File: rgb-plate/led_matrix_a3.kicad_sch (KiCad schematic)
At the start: 32 parts

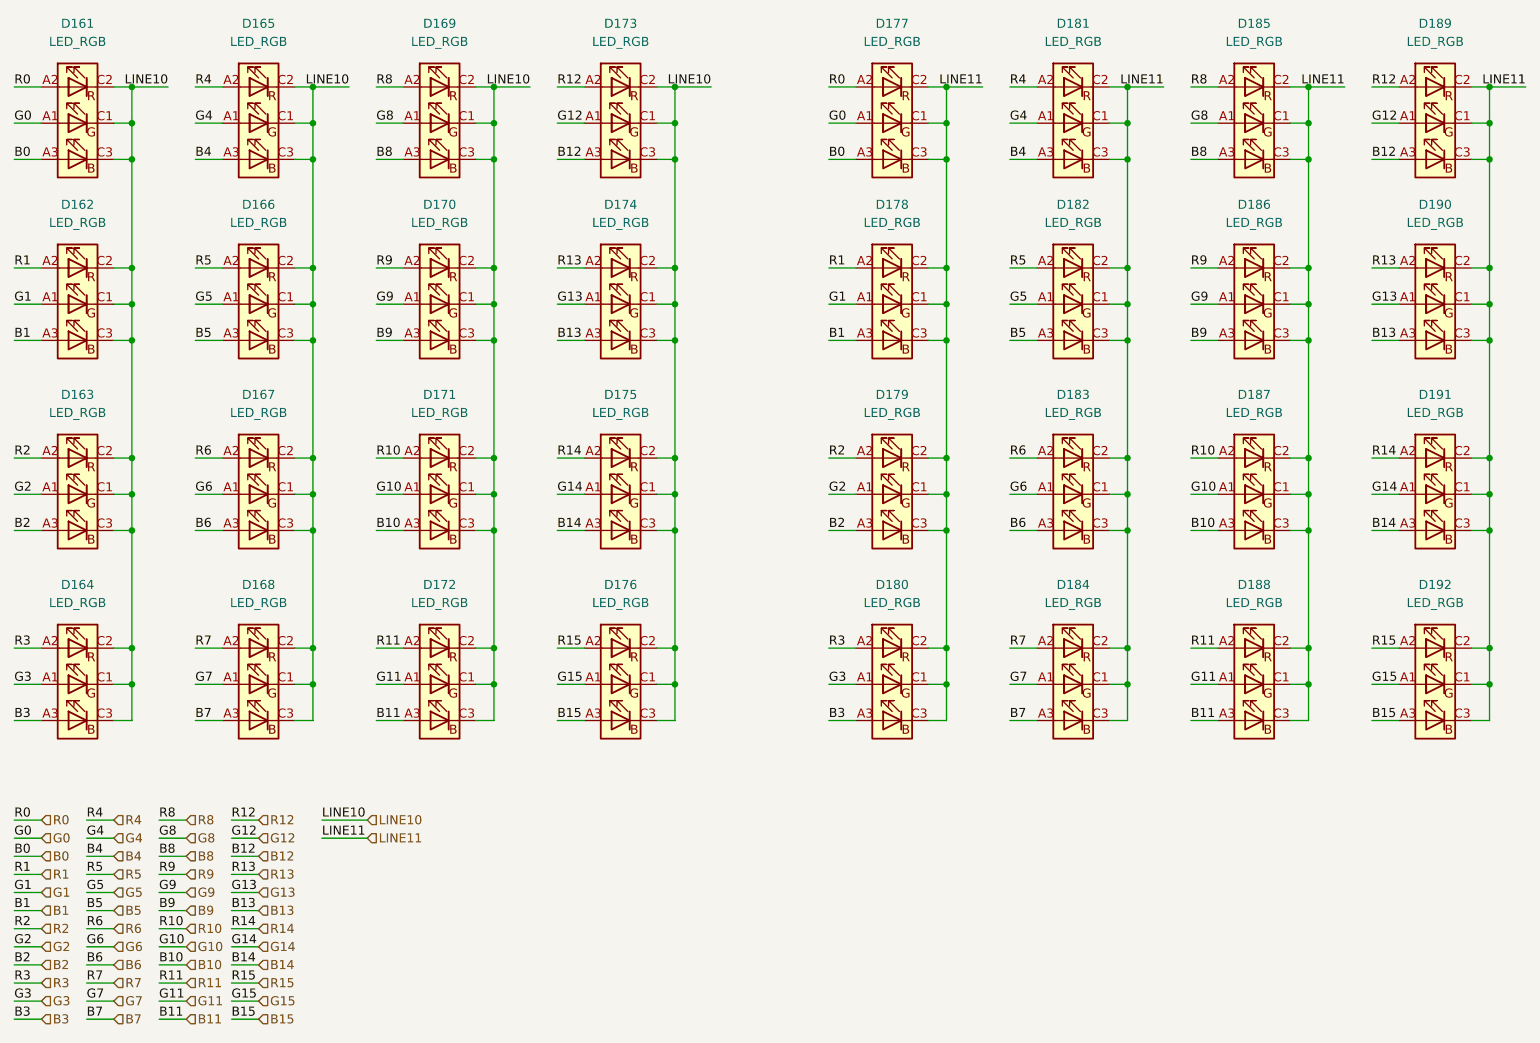
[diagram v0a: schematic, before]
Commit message: initial layout on single board, may need to split up
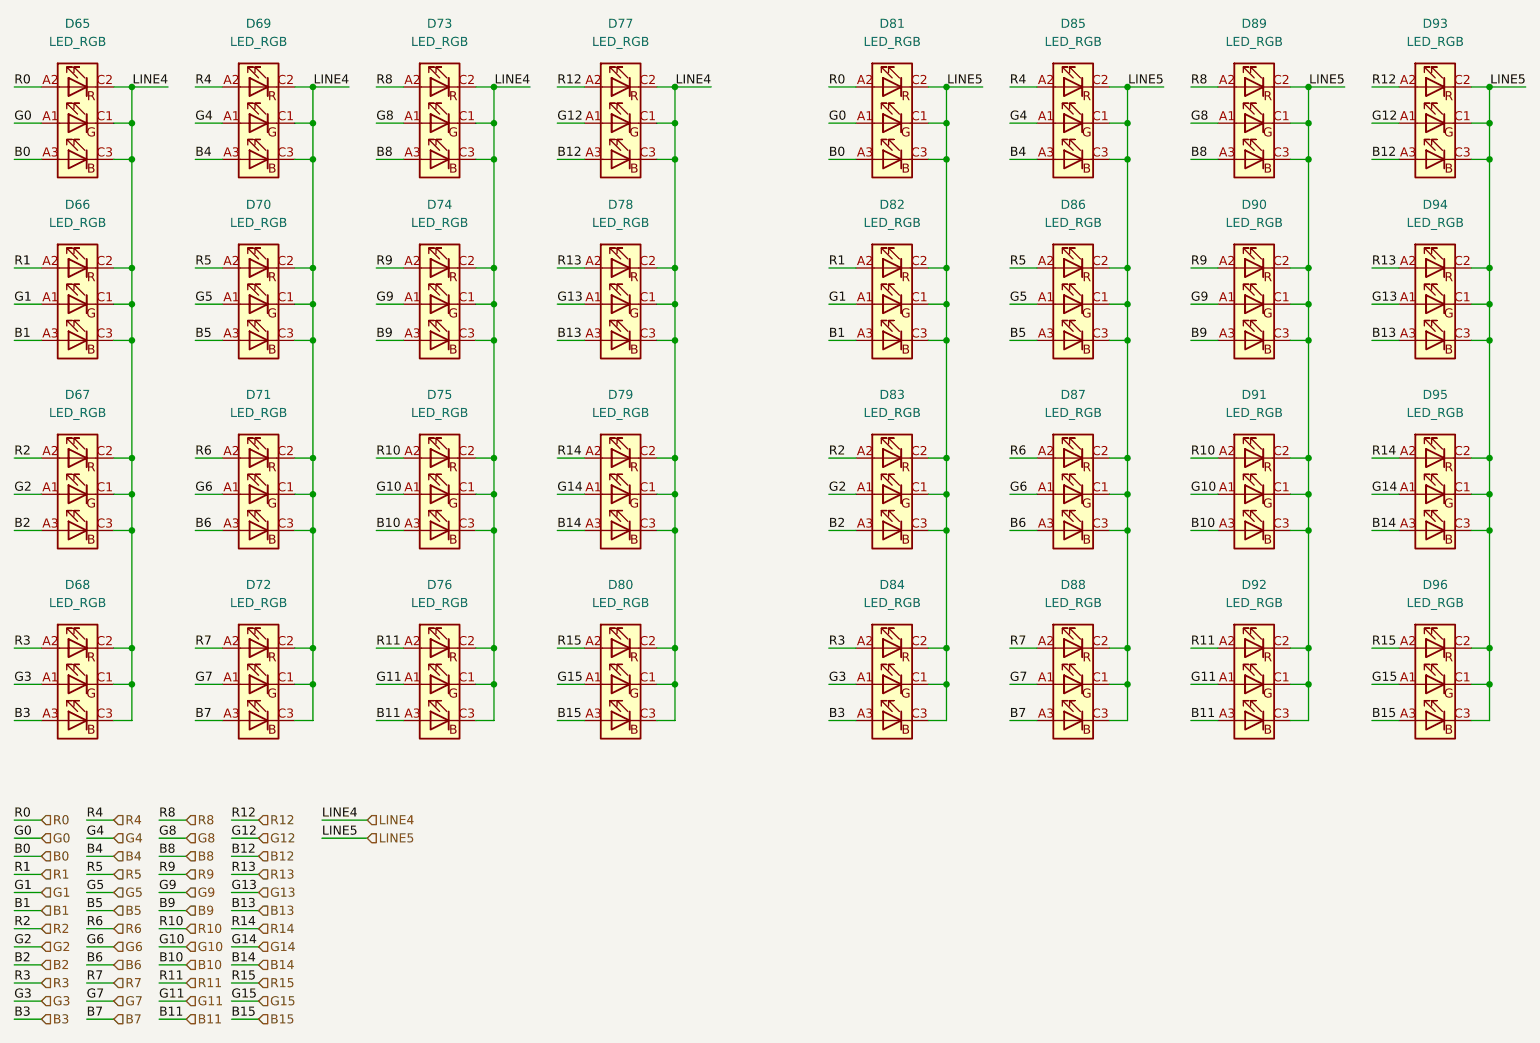
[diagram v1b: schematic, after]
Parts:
- removed D161, D162, D163, D164, D165, D166, D167, D168, D169, D170, D171, D172, D173, D174, D175, D176, D177, D178, D179, D180, D181, D182, D183, D184, D185, D186, D187, D188, D189, D190, D191, D192: LED_RGB, LRTBGVSR-4U4V-JW+8A8B-D8-3S4U-7Z:LRTBGVSR4U4VJW8A8BD83S4U7Z, symbol LRTBGVSR-4U4V-JW+8A8B-D8-3S4U-:LED_RGB
- added D65, D66, D67, D68, D69, D70, D71, D72, D73, D74, D75, D76, D77, D78, D79, D80, D81, D82, D83, D84, D85, D86, D87, D88, D89, D90, D91, D92, D93, D94, D95, D96: LED_RGB, LRTBGVSR-4U4V-JW+8A8B-D8-3S4U-7Z:LRTBGVSR4U4VJW8A8BD83S4U7Z, symbol LRTBGVSR-4U4V-JW+8A8B-D8-3S4U-:LED_RGB
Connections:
- net B0: now also D65.A3 (BA), D81.A3 (BA)
- net B1: now also D66.A3 (BA), D82.A3 (BA)
- net B10: now also D75.A3 (BA), D91.A3 (BA)
- net B11: now also D76.A3 (BA), D92.A3 (BA)
- net B12: now also D77.A3 (BA), D93.A3 (BA)
- net B13: now also D78.A3 (BA), D94.A3 (BA)
- net B14: now also D79.A3 (BA), D95.A3 (BA)
- net B15: now also D80.A3 (BA), D96.A3 (BA)
- net B2: now also D67.A3 (BA), D83.A3 (BA)
- net B3: now also D68.A3 (BA), D84.A3 (BA)
- net B4: now also D69.A3 (BA), D85.A3 (BA)
- net B5: now also D70.A3 (BA), D86.A3 (BA)
- net B6: now also D71.A3 (BA), D87.A3 (BA)
- net B7: now also D72.A3 (BA), D88.A3 (BA)
- net B8: now also D73.A3 (BA), D89.A3 (BA)
- net B9: now also D74.A3 (BA), D90.A3 (BA)
- net G0: now also D65.A1 (GA), D81.A1 (GA)
- net G1: now also D66.A1 (GA), D82.A1 (GA)
- net G10: now also D75.A1 (GA), D91.A1 (GA)
- net G11: now also D76.A1 (GA), D92.A1 (GA)
- net G12: now also D77.A1 (GA), D93.A1 (GA)
- net G13: now also D78.A1 (GA), D94.A1 (GA)
- net G14: now also D79.A1 (GA), D95.A1 (GA)
- net G15: now also D80.A1 (GA), D96.A1 (GA)
- net G2: now also D67.A1 (GA), D83.A1 (GA)
- net G3: now also D68.A1 (GA), D84.A1 (GA)
- net G4: now also D69.A1 (GA), D85.A1 (GA)
- net G5: now also D70.A1 (GA), D86.A1 (GA)
- net G6: now also D71.A1 (GA), D87.A1 (GA)
- net G7: now also D72.A1 (GA), D88.A1 (GA)
- net G8: now also D73.A1 (GA), D89.A1 (GA)
- net G9: now also D74.A1 (GA), D90.A1 (GA)
- net R0: now also D65.A2 (RA), D81.A2 (RA)
- net R1: now also D66.A2 (RA), D82.A2 (RA)
- net R10: now also D75.A2 (RA), D91.A2 (RA)
- net R11: now also D76.A2 (RA), D92.A2 (RA)
- net R12: now also D77.A2 (RA), D93.A2 (RA)
- net R13: now also D78.A2 (RA), D94.A2 (RA)
- net R14: now also D79.A2 (RA), D95.A2 (RA)
- net R15: now also D80.A2 (RA), D96.A2 (RA)
- net R2: now also D67.A2 (RA), D83.A2 (RA)
- net R3: now also D68.A2 (RA), D84.A2 (RA)
- net R4: now also D69.A2 (RA), D85.A2 (RA)
- net R5: now also D70.A2 (RA), D86.A2 (RA)
- net R6: now also D71.A2 (RA), D87.A2 (RA)
- net R7: now also D72.A2 (RA), D88.A2 (RA)
- net R8: now also D73.A2 (RA), D89.A2 (RA)
- net R9: now also D74.A2 (RA), D90.A2 (RA)
- new net LINE4: D65.C1 (GK), D65.C2 (RK), D65.C3 (BK), D66.C1 (GK), D66.C2 (RK), D66.C3 (BK), D67.C1 (GK), D67.C2 (RK), D67.C3 (BK), D68.C1 (GK), D68.C2 (RK), D68.C3 (BK), D69.C1 (GK), D69.C2 (RK), D69.C3 (BK), D70.C1 (GK), D70.C2 (RK), D70.C3 (BK), D71.C1 (GK), D71.C2 (RK), D71.C3 (BK), D72.C1 (GK), D72.C2 (RK), D72.C3 (BK), D73.C1 (GK), D73.C2 (RK), D73.C3 (BK), D74.C1 (GK), D74.C2 (RK), D74.C3 (BK), D75.C1 (GK), D75.C2 (RK), D75.C3 (BK), D76.C1 (GK), D76.C2 (RK), D76.C3 (BK), D77.C1 (GK), D77.C2 (RK), D77.C3 (BK), D78.C1 (GK), D78.C2 (RK), D78.C3 (BK), D79.C1 (GK), D79.C2 (RK), D79.C3 (BK), D80.C1 (GK), D80.C2 (RK), D80.C3 (BK)
- new net LINE5: D81.C1 (GK), D81.C2 (RK), D81.C3 (BK), D82.C1 (GK), D82.C2 (RK), D82.C3 (BK), D83.C1 (GK), D83.C2 (RK), D83.C3 (BK), D84.C1 (GK), D84.C2 (RK), D84.C3 (BK), D85.C1 (GK), D85.C2 (RK), D85.C3 (BK), D86.C1 (GK), D86.C2 (RK), D86.C3 (BK), D87.C1 (GK), D87.C2 (RK), D87.C3 (BK), D88.C1 (GK), D88.C2 (RK), D88.C3 (BK), D89.C1 (GK), D89.C2 (RK), D89.C3 (BK), D90.C1 (GK), D90.C2 (RK), D90.C3 (BK), D91.C1 (GK), D91.C2 (RK), D91.C3 (BK), D92.C1 (GK), D92.C2 (RK), D92.C3 (BK), D93.C1 (GK), D93.C2 (RK), D93.C3 (BK), D94.C1 (GK), D94.C2 (RK), D94.C3 (BK), D95.C1 (GK), D95.C2 (RK), D95.C3 (BK), D96.C1 (GK), D96.C2 (RK), D96.C3 (BK)
